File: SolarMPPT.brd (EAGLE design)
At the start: 100 x 80 mm, 42 parts, among them J1 CORTEX_DEBUG_SMD, U1 STM32F091CCT6, U3 LTC1155, U6 3.3V, U7 LM22674MRX-5.0

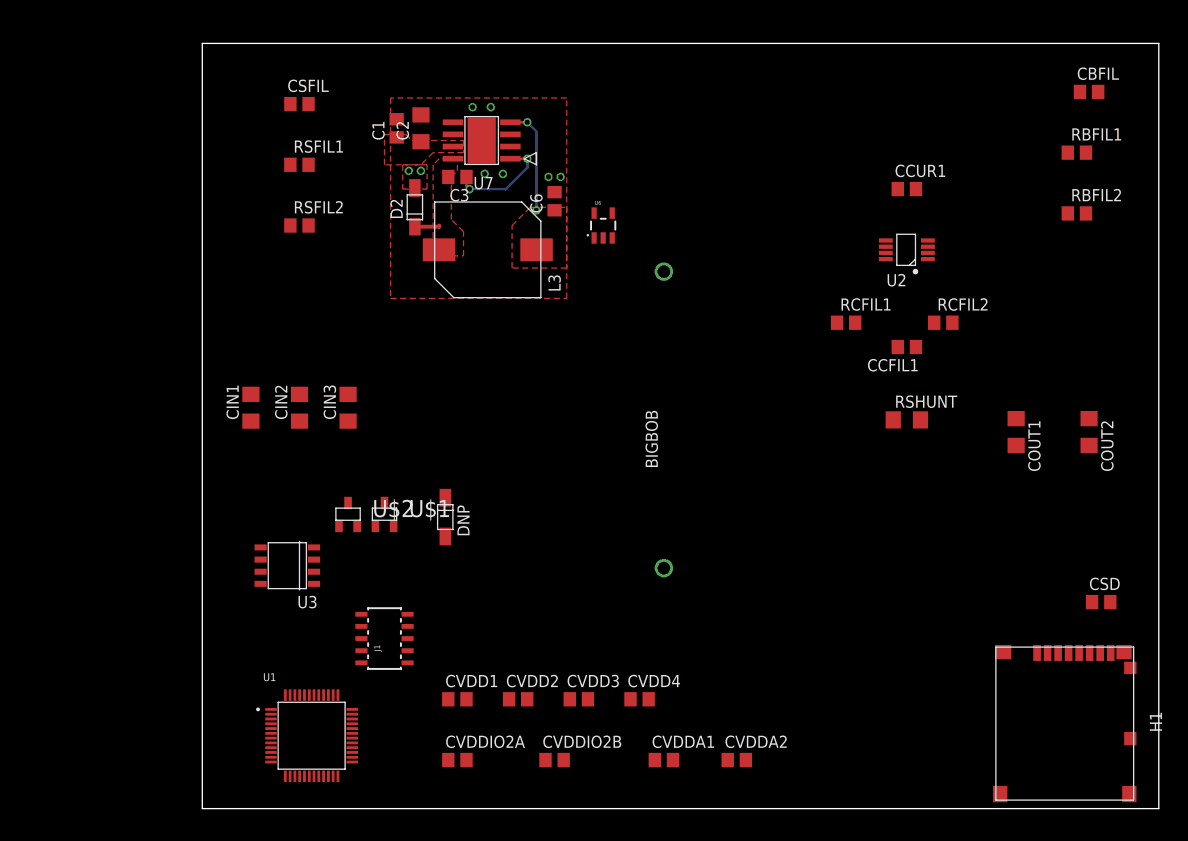
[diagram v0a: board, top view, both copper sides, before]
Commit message: placed components in rough location. Might remap ADC pins for routing
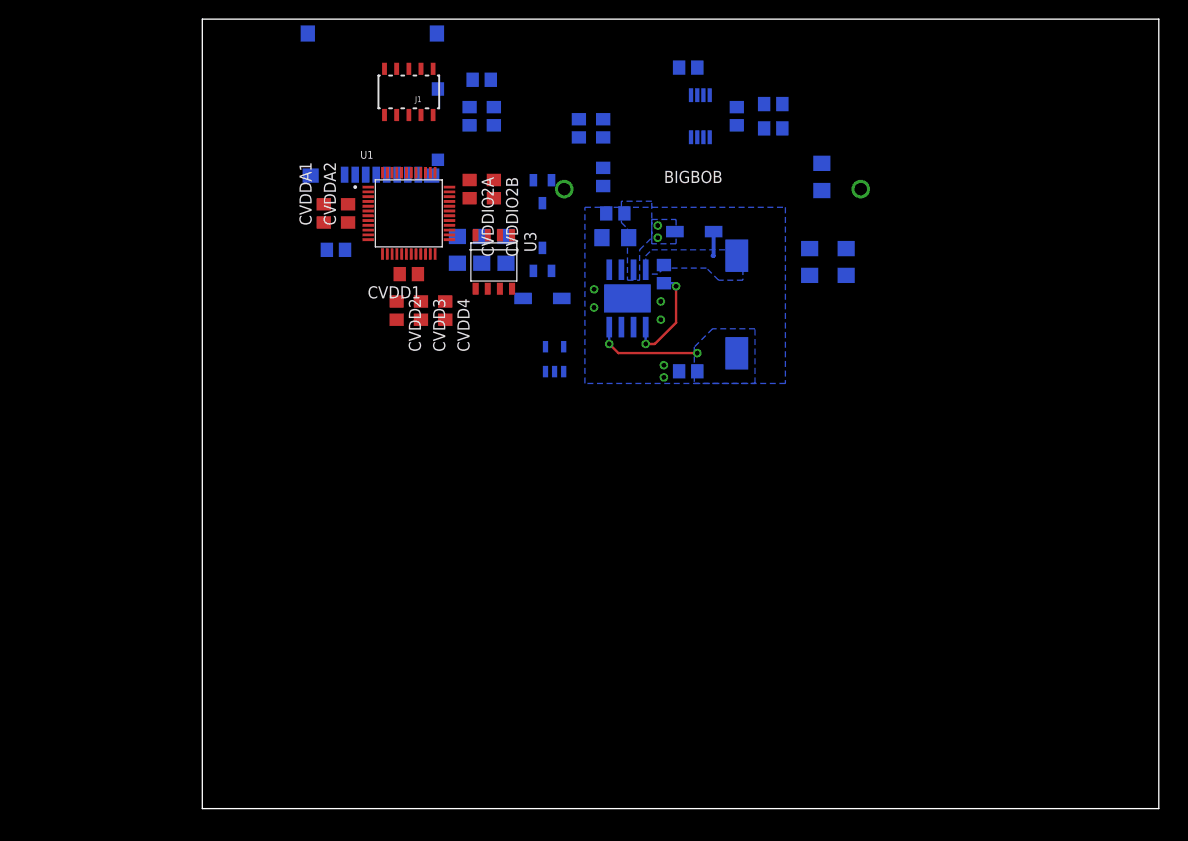
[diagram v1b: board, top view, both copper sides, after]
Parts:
- moved H1 97.1 mm to (17.8, 73.7), flipped to the bottom, turned to 0 degrees
- moved CSD 88.1 mm to (14.0, 58.4), flipped to the bottom
- moved CVDDA2 70.1 mm to (15.2, 62.2), turned to 90 degrees
- moved CVDDA1 67.3 mm to (12.7, 62.2), turned to 90 degrees
- moved CVDDIO2B 60.0 mm to (30.5, 64.8), turned to 270 degrees
- moved CVDDIO2A 59.7 mm to (27.9, 64.8), turned to 270 degrees
- moved J1 57.2 mm to (21.6, 74.9), turned to 180 degrees
- moved U1 55.5 mm to (21.6, 62.2)
- moved CBFIL 53.5 mm to (39.4, 71.1), flipped to the bottom, turned to 90 degrees
- moved RBFIL2 50.3 mm to (41.9, 71.1), flipped to the bottom, turned to 270 degrees
- moved RBFIL1 49.6 mm to (41.9, 66.0), flipped to the bottom, turned to 270 degrees
- moved CVDD4 45.4 mm to (25.4, 52.1), turned to 270 degrees
- moved CVDD1 44.7 mm to (21.6, 55.9), turned to 180 degrees
- moved CVDD3 43.9 mm to (22.9, 52.1), turned to 270 degrees
- moved CVDD2 42.6 mm to (20.3, 52.1), turned to 270 degrees
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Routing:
- added copper zone on layer 16, net +5V
- added copper zone on layer 16, net GND
- added copper zone on layer 16, net SW_5V2
- added copper zone on layer 16, net VCC
- removed copper zone on layer 1, net +5V
- removed copper zone on layer 1, net GND
- removed copper zone on layer 1, net SW_5V2
- removed copper zone on layer 1, net VCC
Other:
- board size 100 x 80 mm -> 100 x 82.5 mm

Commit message: Did power routing and added terminals
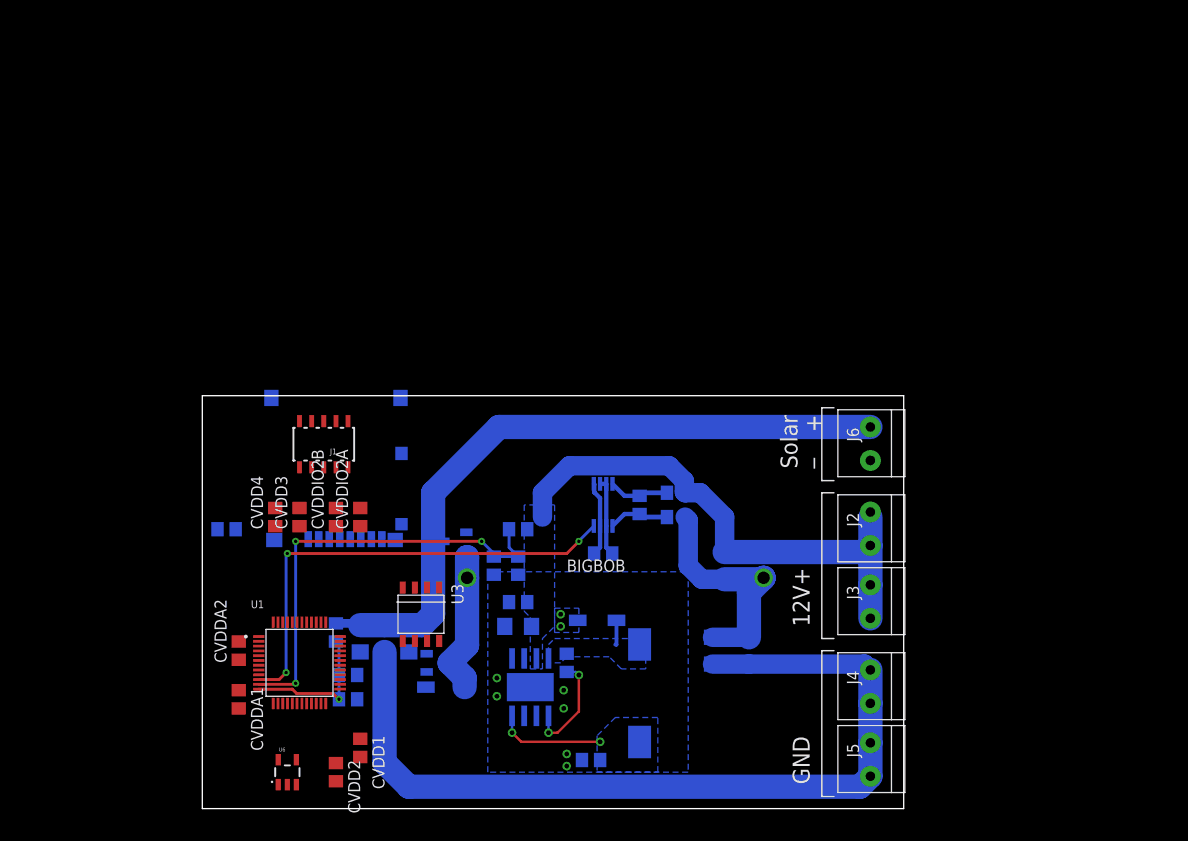
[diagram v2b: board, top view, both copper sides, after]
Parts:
- added J2, J3, J4, J5, J6: 1X2-3.5MM, adafruit:1X2-3.5MM
- CVDD2: value 100nF -> 4.7uF
- moved RSFIL2 62.3 mm to (15.2, 11.4), turned to 0 degrees
- moved CSFIL 60.4 mm to (15.2, 14.0), turned to 180 degrees
- moved RSFIL1 59.8 mm to (14.0, 18.4), turned to 90 degrees
- moved CCUR1 51.6 mm to (41.9, 26.7)
- moved CVDDA1 51.6 mm to (3.81, 11.4), turned to 270 degrees
- moved U6 51.4 mm to (8.89, 3.81), flipped to the top
- moved CVDD1 49.8 mm to (16.5, 6.35), turned to 270 degrees
- moved CVDD2 48.7 mm to (14.0, 3.81)
- moved U1 48.4 mm to (10.2, 15.2)
- moved CVDDA2 47.1 mm to (3.81, 16.5)
- moved CBFIL 46.6 mm to (30.5, 25.4), turned to 270 degrees
- moved RBFIL2 46.6 mm to (33.0, 25.4), turned to 90 degrees
- moved U$2 43.4 mm to (24.4, 15.2), turned to 90 degrees
- moved RSHUNT 41.9 mm to (54.6, 25.4)
- moved BIGBOB 41.9 mm to (43.2, 24.1)
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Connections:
- net +12V: now also J2.1, J2.2, J3.1, J3.2
- net +18V: now also J6.1
- net GND: now also J4.1, J4.2, J5.1, J5.2, J6.2
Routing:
- net GND: track 0.00 -> 99.9 mm
- net +18V: track 0.00 -> 72.0 mm
- net +12V: track 0.00 -> 55.4 mm
- net CURR_SENS: track 0.00 -> 48.9 mm, vias 0 -> 3
- net BATT_SENS: track 0.00 -> 46.1 mm, vias 0 -> 3
- net N$10: track 0.00 -> 24.4 mm
- net N$7: track 0.00 -> 15.0 mm
- net SOLAR_SENS: track 0.00 -> 15.0 mm, vias 0 -> 1
- net +3V3: track 0.00 -> 8.40 mm
- net N$6: track 0.00 -> 6.35 mm
- net N$5: track 0.00 -> 6.35 mm
- added copper zone on layer 16, net +12V
- removed copper zone on layer 16, net VCC
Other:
- board size 100 x 82.5 mm -> 73.3 x 43.2 mm
- board text added: "+"
- board text added: "12V+"
- board text added: "GND"
- board text added: "Solar"
- board text added: "_"

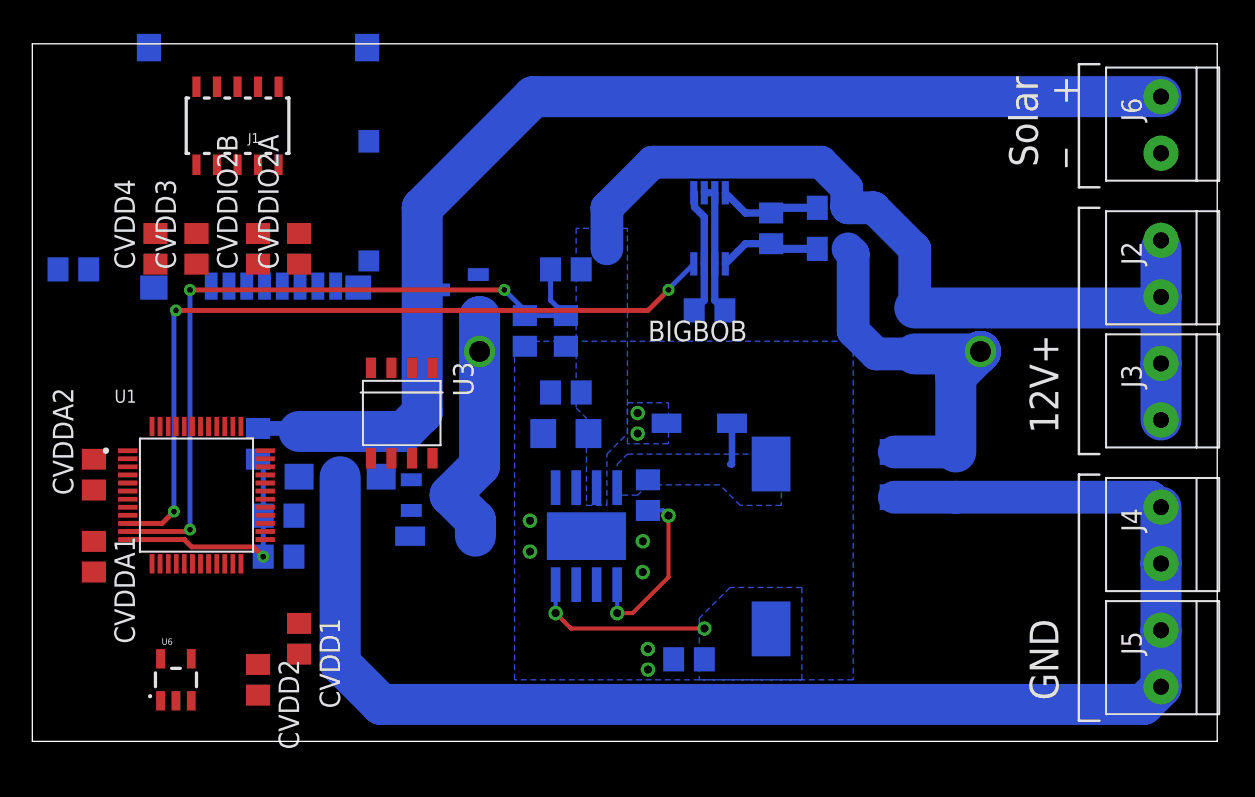
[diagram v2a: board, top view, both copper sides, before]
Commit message: added teensy, removed SD
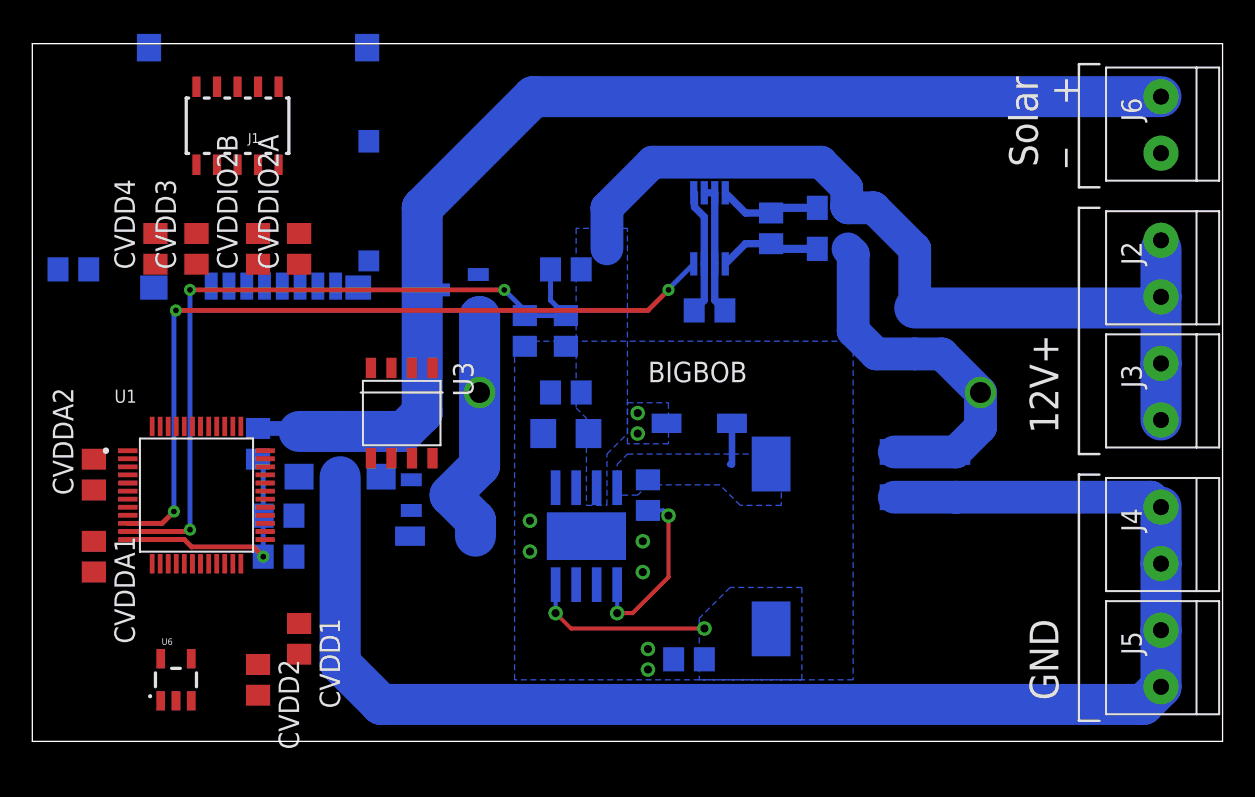
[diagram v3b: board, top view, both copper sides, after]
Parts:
- moved BIGBOB 2.54 mm to (43.2, 21.6)
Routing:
- net N$10: track 24.4 -> 22.8 mm
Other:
- board size 73.3 x 43.2 mm -> 73.7 x 43.2 mm
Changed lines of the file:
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@@
 <board>
 <plain>
-<wire x1="0" y1="0" x2="73.33" y2="0" width="0" layer="20"/>
-<wire x1="73.33" y1="0" x2="73.33" y2="43.17" width="0" layer="20"/>
-<wire x1="73.33" y1="43.17" x2="0" y2="43.17" width="0" layer="20"/>
-<wire x1="0" y1="43.17" x2="0" y2="0" width="0" layer="20"/>
+<wire x1="0" y1="0" x2="73.66" y2="0" width="0" layer="20"/>
+<wire x1="73.66" y1="0" x2="73.66" y2="43.18" width="0" layer="20"/>
+<wire x1="73.66" y1="43.18" x2="0" y2="43.18" width="0" layer="20"/>
+<wire x1="0" y1="43.18" x2="0" y2="0" width="0" layer="20"/>
 <text x="62.23" y="35.56" size="1.778" layer="21" rot="R90">Solar</text>
 <text x="63.5" y="19.05" size="1.778" layer="21" rot="R90">12V+</text>
@@
 <attribute name="VALUE" x="14.4018" y="39.0652" size="0.6096" layer="27" font="vector" ratio="20" rot="R180"/>
 </element>
-<element name="BIGBOB" library="rcl" library_urn="urn:adsk.eagle:library:334" package="TJ6-U2" package3d_urn="urn:adsk.eagle:package:23510/1" value="390uH" x="43.18" y="24.13" smashed="yes">
-<attribute name="NAME" x="38.1" y="24.765" size="1.27" layer="25"/>
-<attribute name="POPULARITY" value="0" x="73.66" y="6.35" size="1.778" layer="27" display="off"/>
-<attribute name="SPICEPREFIX" value="L" x="73.66" y="6.35" size="1.778" layer="27" display="off"/>
-<attribute name="VALUE" x="38.1" y="22.225" size="1.27" layer="27"/>
+<element name="BIGBOB" library="rcl" library_urn="urn:adsk.eagle:library:334" package="TJ6-U2" package3d_urn="urn:adsk.eagle:package:23510/1" value="390uH" x="43.18" y="21.59" smashed="yes">
+<attribute name="NAME" x="38.1" y="22.225" size="1.27" layer="25"/>
+<attribute name="POPULARITY" value="0" x="73.66" y="3.81" size="1.778" layer="27" display="off"/>
+<attribute name="SPICEPREFIX" value="L" x="73.66" y="3.81" size="1.778" layer="27" display="off"/>
+<attribute name="VALUE" x="38.1" y="19.685" size="1.27" layer="27"/>
 </element>
 <element name="RBFIL1" library="rcl" library_urn="urn:adsk.eagle:library:334" package="R0805" package3d_urn="urn:adsk.eagle:package:23553/2" value="180k" x="33.02" y="29.21" smashed="yes" rot="MR180">
@@
 <contactref element="DNP" pad="K"/>
 <wire x1="25.854" y1="15.24" x2="27.68" y2="17.066" width="2.54" layer="16"/>
-<wire x1="27.68" y1="17.066" x2="27.68" y2="24.13" width="2.54" layer="16"/>
+<wire x1="27.68" y1="17.066" x2="27.68" y2="21.59" width="2.54" layer="16"/>
 <wire x1="27.425" y1="12.7" x2="27.425" y2="13.669" width="2.54" layer="16"/>
 <wire x1="27.425" y1="13.669" x2="25.854" y2="15.24" width="2.54" layer="16"/>
-<wire x1="27.68" y1="24.13" x2="27.68" y2="26.283" width="2.54" layer="16"/>
+<wire x1="27.68" y1="21.59" x2="27.68" y2="26.283" width="2.54" layer="16"/>
 <wire x1="27.68" y1="26.283" x2="27.686" y2="26.289" width="2.54" layer="16"/>
 <wire x1="27.686" y1="26.289" x2="27.6" y2="26.99" width="0" layer="19" extent="16-16"/>
@@
 <contactref element="RCFIL1" pad="2"/>
 <contactref element="RSHUNT" pad="1"/>
-<wire x1="58.68" y1="24.13" x2="57.15" y2="22.6" width="2.54" layer="16"/>
-<wire x1="57.15" y1="22.6" x2="57.15" y2="17.91" width="2.54" layer="16"/>
 <wire x1="53.34" y1="17.91" x2="57.15" y2="17.91" width="2.032" layer="16"/>
-<wire x1="54.61" y1="23.978" x2="58.528" y2="23.978" width="2.54" layer="16"/>
-<wire x1="58.528" y1="23.978" x2="58.6796" y2="24.1296" width="2.54" layer="16"/>
-<wire x1="58.6796" y1="24.1296" x2="58.68" y2="24.1296" width="2.54" layer="16"/>
 <wire x1="50.48" y1="30.48" x2="50.8" y2="30.16" width="2.032" layer="16"/>
 <wire x1="50.8" y1="30.16" x2="50.8" y2="25.4" width="2.032" layer="16"/>
 <wire x1="50.8" y1="25.4" x2="52.222" y2="23.978" width="2.032" layer="16"/>
 <wire x1="52.222" y1="23.978" x2="54.61" y2="23.978" width="2.032" layer="16"/>
-<wire x1="58.68" y1="24.13" x2="58.68" y2="24.1296" width="0" layer="19" extent="16-16"/>
+<wire x1="57.15" y1="17.91" x2="58.68" y2="19.44" width="2.032" layer="16"/>
+<wire x1="58.68" y1="19.44" x2="58.68" y2="21.59" width="2.032" layer="16"/>
+<wire x1="58.68" y1="21.59" x2="56.292" y2="23.978" width="2.032" layer="16"/>
+<wire x1="56.292" y1="23.978" x2="54.61" y2="23.978" width="2.032" layer="16"/>
 </signal>
 <signal name="BOOT_5V2">
